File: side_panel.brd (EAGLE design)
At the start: 81.7 x 112 mm, 47 parts

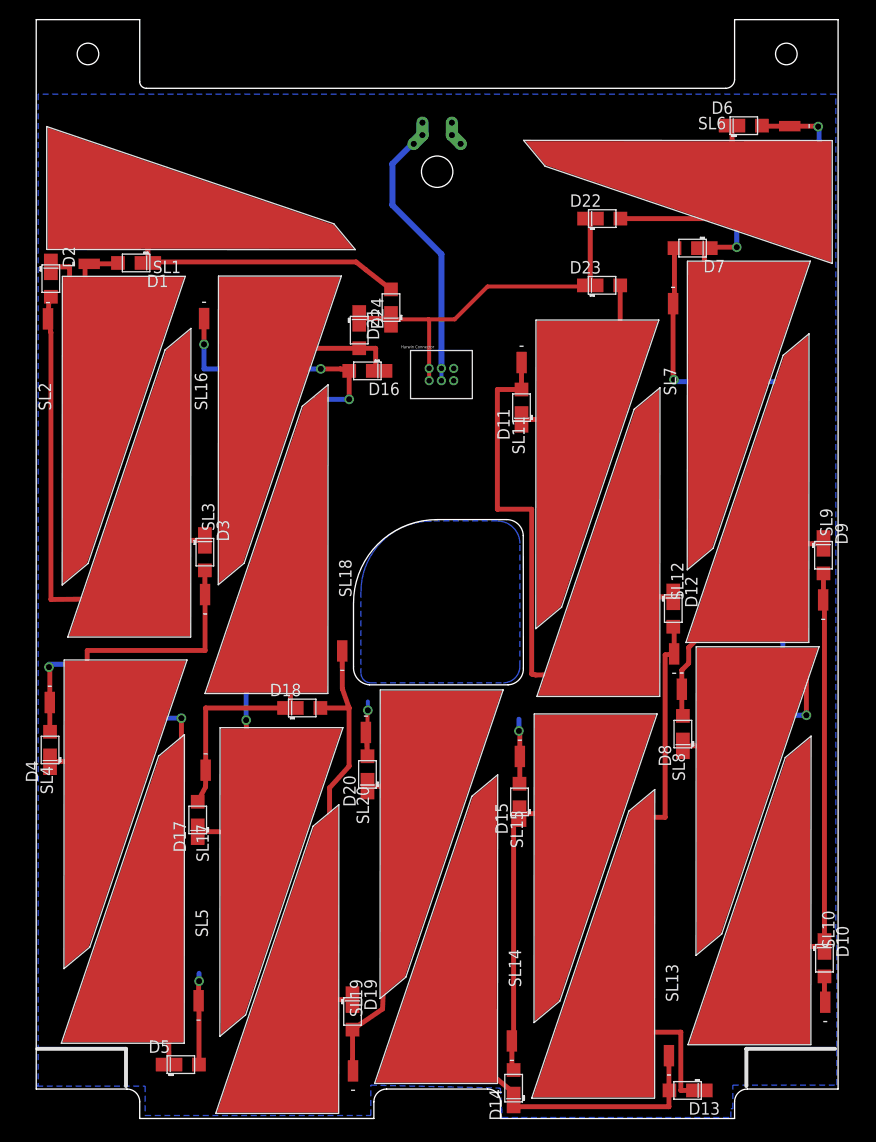
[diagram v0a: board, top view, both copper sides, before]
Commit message: Fixed manufacturing issue on TASC cell footprint
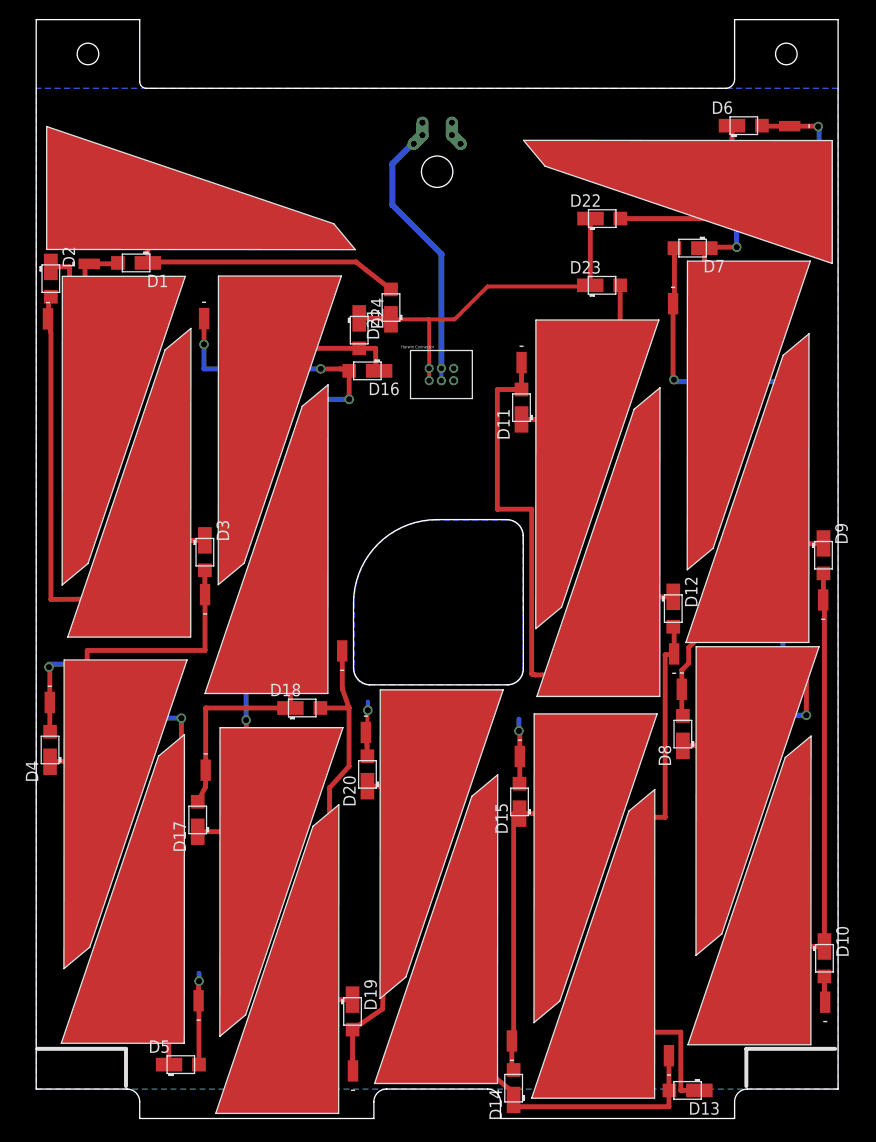
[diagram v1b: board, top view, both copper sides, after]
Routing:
- added copper zone on layer 16, net N$10
- added copper zone on layer 16, net N$12
- removed copper zone on layer 16, net GND
- removed copper zone on layer 16, net N$13
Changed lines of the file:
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@@
 <layers>
 <layer number="1" name="Top" color="4" fill="1" visible="yes" active="yes"/>
+<layer number="2" name="Route2" color="1" fill="3" visible="no" active="no"/>
+<layer number="3" name="Route3" color="4" fill="3" visible="no" active="no"/>
+<layer number="14" name="Route14" color="1" fill="6" visible="no" active="no"/>
+<layer number="15" name="Route15" color="4" fill="6" visible="no" active="no"/>
 <layer number="16" name="Bottom" color="1" fill="1" visible="yes" active="yes"/>
 <layer number="17" name="Pads" color="2" fill="1" visible="yes" active="yes"/>
@@
 <contactref element="SL20" pad="1"/>
 <contactref element="D20" pad="POS"/>
-<polygon width="0" layer="16" thermals="no">
-<vertex x="0.1" y="3.3"/>
-<vertex x="11.1" y="3.3"/>
-<vertex x="11.1" y="0.3"/>
-<vertex x="34.1" y="0.3"/>
-<vertex x="34.1" y="3.4"/>
-<vertex x="47.3" y="3.1"/>
-<vertex x="47.5" y="0.1"/>
-<vertex x="70.8" y="0.1"/>
-<vertex x="70.8" y="1"/>
-<vertex x="71" y="1"/>
-<vertex x="71" y="3.4"/>
-<vertex x="81.6" y="3.4"/>
-<vertex x="81.6" y="19.2"/>
-<vertex x="81.5" y="19.2"/>
-<vertex x="81.5" y="104.4"/>
-<vertex x="0.2" y="104.4"/>
-<vertex x="0.2" y="3.4"/>
-</polygon>
 <wire x1="33.76" y1="36.92" x2="33.66" y2="38.6491" width="0.5" layer="1"/>
 <wire x1="33.66" y1="38.6491" x2="33.6007" y2="39.3491" width="0.5" layer="1"/>
@@
 <contactref element="U$2" pad="H3"/>
 <contactref element="U$2" pad="H1"/>
+<wire x1="42.365" y1="100.23" x2="43.254" y2="99.341" width="0" layer="19" extent="1-1"/>
+<wire x1="42.365" y1="101.5" x2="42.365" y2="100.23" width="0" layer="19" extent="1-1"/>
+<wire x1="42.55" y1="76.45" x2="43.254" y2="99.341" width="0" layer="19" extent="1-1"/>
+<wire x1="42.55" y1="75.2" x2="42.55" y2="76.45" width="0" layer="19" extent="1-1"/>
+<wire x1="33.8" y1="42.5" x2="42.55" y2="75.2" width="0" layer="19" extent="16-16"/>
+<wire x1="49.2" y1="40.7" x2="33.8" y2="41.6" width="0" layer="19" extent="16-16"/>
+<wire x1="16.6" y1="14.8" x2="33.76" y2="36.92" width="0" layer="19" extent="1-16"/>
 </signal>
 <signal name="N$36">
@@
 <wire x1="80.34" y1="11.8509" x2="80.34" y2="14.48" width="0.5" layer="1"/>
 </signal>
-<signal name="N$13">
-<polygon width="0" layer="16" pour="cutout">
-<vertex x="33.1" y="45.9"/>
-<vertex x="33.1" y="45.4" curve="90"/>
-<vertex x="34.1" y="44.4"/>
-<vertex x="47.6" y="44.4" curve="90"/>
-<vertex x="49.3" y="46.1"/>
-<vertex x="49.3" y="58.6" curve="90"/>
-<vertex x="47" y="60.9"/>
-<vertex x="40.3" y="60.9" curve="90"/>
-<vertex x="33.1" y="53.7"/>
-</polygon>
-</signal>
 <signal name="V_BURN">
 <contactref element="U$1" pad="P5"/>
@@
 <wire x1="41.3" y1="88.1" x2="41.3" y2="76.45" width="0.6096" layer="16"/>
 </signal>
+<signal name="N$10">
+<polygon width="0.254" layer="16">
+<vertex x="0" y="3"/>
+<vertex x="81.73" y="3"/>
+<vertex x="81.73" y="105"/>
+<vertex x="0" y="105"/>
+</polygon>
+</signal>
+<signal name="N$12">
+<polygon width="0.254" layer="16" pour="cutout">
+<vertex x="34" y="44.2"/>
+<vertex x="48" y="44.2" curve="90"/>
+<vertex x="49.6" y="45.8"/>
+<vertex x="49.6" y="59.2"/>
+<vertex x="49.6" y="59.4" curve="90"/>
+<vertex x="48" y="61"/>
+<vertex x="40.9" y="61"/>
+<vertex x="40.8" y="61" curve="90"/>
+<vertex x="32.4" y="52.6"/>
+<vertex x="32.4" y="46"/>
+<vertex x="32.4" y="45.7" curve="90"/>
+<vertex x="33.9" y="44.2"/>
+</polygon>
+</signal>
 </signals>

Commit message: Fixed solar panel issue
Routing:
- added copper zone on layer 16, net GND
- removed copper zone on layer 16, net N$10
- removed copper zone on layer 16, net N$12
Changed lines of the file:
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@@
 <?xml version="1.0" encoding="utf-8"?>
 <!DOCTYPE eagle SYSTEM "eagle.dtd">
-<eagle version="6.5.0">
+<eagle version="6.6.0">
 <drawing>
 <settings>
@@
 <contactref element="U$2" pad="H3"/>
 <contactref element="U$2" pad="H1"/>
+<polygon width="0.254" layer="16">
+<vertex x="0" y="3"/>
+<vertex x="81.73" y="3"/>
+<vertex x="81.73" y="105"/>
+<vertex x="0" y="105"/>
+</polygon>
+<polygon width="0.254" layer="16" pour="cutout">
+<vertex x="34" y="44.2"/>
+<vertex x="48" y="44.2" curve="90"/>
+<vertex x="49.6" y="45.8"/>
+<vertex x="49.6" y="59.2"/>
+<vertex x="49.6" y="59.4" curve="90"/>
+<vertex x="48" y="61"/>
+<vertex x="40.9" y="61"/>
+<vertex x="40.8" y="61" curve="90"/>
+<vertex x="32.4" y="52.6"/>
+<vertex x="32.4" y="46"/>
+<vertex x="32.4" y="45.7" curve="90"/>
+<vertex x="33.9" y="44.2"/>
+</polygon>
 <wire x1="42.365" y1="100.23" x2="43.254" y2="99.341" width="0" layer="19" extent="1-1"/>
 <wire x1="42.365" y1="101.5" x2="42.365" y2="100.23" width="0" layer="19" extent="1-1"/>
-<wire x1="42.55" y1="76.45" x2="43.254" y2="99.341" width="0" layer="19" extent="1-1"/>
-<wire x1="42.55" y1="75.2" x2="42.55" y2="76.45" width="0" layer="19" extent="1-1"/>
-<wire x1="33.8" y1="42.5" x2="42.55" y2="75.2" width="0" layer="19" extent="16-16"/>
-<wire x1="49.2" y1="40.7" x2="33.8" y2="41.6" width="0" layer="19" extent="16-16"/>
-<wire x1="16.6" y1="14.8" x2="33.76" y2="36.92" width="0" layer="19" extent="1-16"/>
 </signal>
 <signal name="N$36">
@@
 <wire x1="41.3" y1="88.1" x2="41.3" y2="76.45" width="0.6096" layer="16"/>
 </signal>
-<signal name="N$10">
-<polygon width="0.254" layer="16">
-<vertex x="0" y="3"/>
-<vertex x="81.73" y="3"/>
-<vertex x="81.73" y="105"/>
-<vertex x="0" y="105"/>
-</polygon>
-</signal>
-<signal name="N$12">
-<polygon width="0.254" layer="16" pour="cutout">
-<vertex x="34" y="44.2"/>
-<vertex x="48" y="44.2" curve="90"/>
-<vertex x="49.6" y="45.8"/>
-<vertex x="49.6" y="59.2"/>
-<vertex x="49.6" y="59.4" curve="90"/>
-<vertex x="48" y="61"/>
-<vertex x="40.9" y="61"/>
-<vertex x="40.8" y="61" curve="90"/>
-<vertex x="32.4" y="52.6"/>
-<vertex x="32.4" y="46"/>
-<vertex x="32.4" y="45.7" curve="90"/>
-<vertex x="33.9" y="44.2"/>
-</polygon>
-</signal>
 </signals>

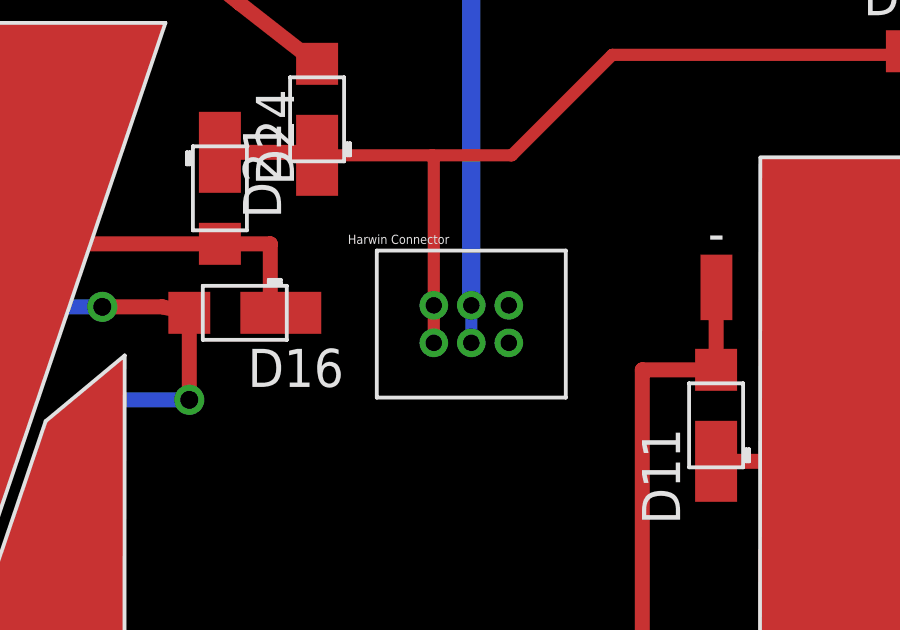
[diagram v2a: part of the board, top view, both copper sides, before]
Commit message: Updated Gecko Connector
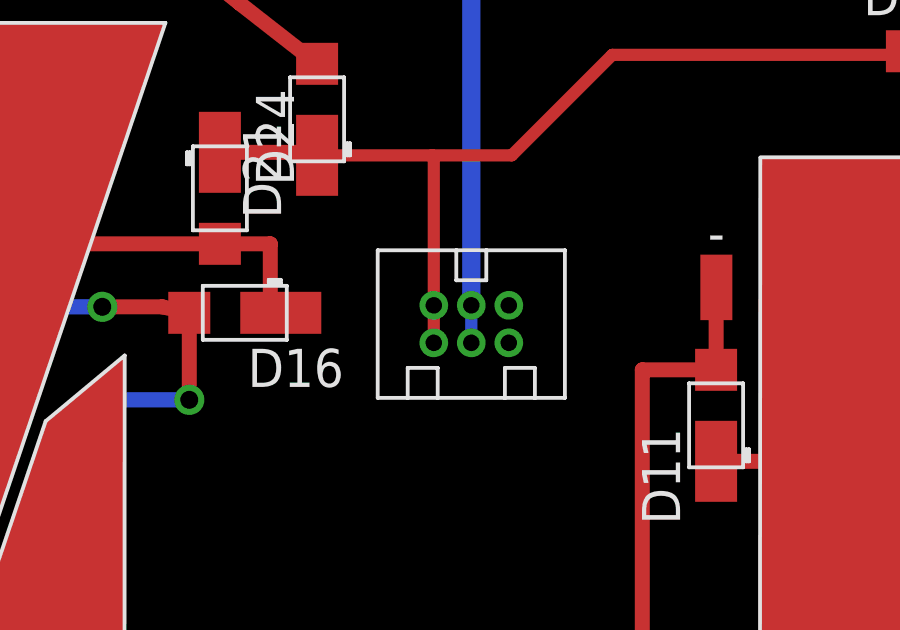
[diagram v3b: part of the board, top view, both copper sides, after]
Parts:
- moved U$1 0.10 mm to (38.2, 73.4)
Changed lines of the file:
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@@
 <element name="D20" library="phonesat" package="SB_DIODE" value="SB_DIODE" x="33.76" y="35.07" rot="R90"/>
 <element name="D24" library="phonesat" package="SB_DIODE" value="SB_DIODE" x="32.92" y="80.35" rot="R270"/>
-<element name="U$1" library="G125-FV20605L0P" package="G125-FV20605L0P" value="G125-FV20605L0P" x="38.1" y="73.3"/>
+<element name="U$1" library="G125-FV20605L0P" package="G125-FV20605L0P" value="G125-FV20605L0P" x="38.18" y="73.365"/>
 <element name="U$4" library="Burner" package="BURNER" value="BURNER" x="39.365" y="101.5" rot="MR270"/>
 <element name="U$2" library="Burner" package="BURNER" value="BURNER" x="42.365" y="101.5" rot="R270"/>

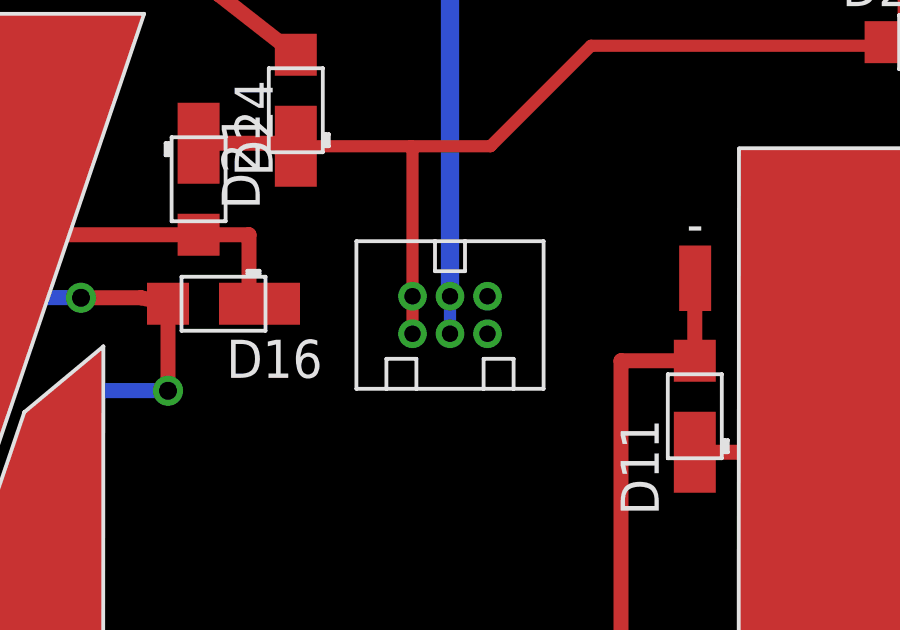
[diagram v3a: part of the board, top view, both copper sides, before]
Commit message: Finished main board layout
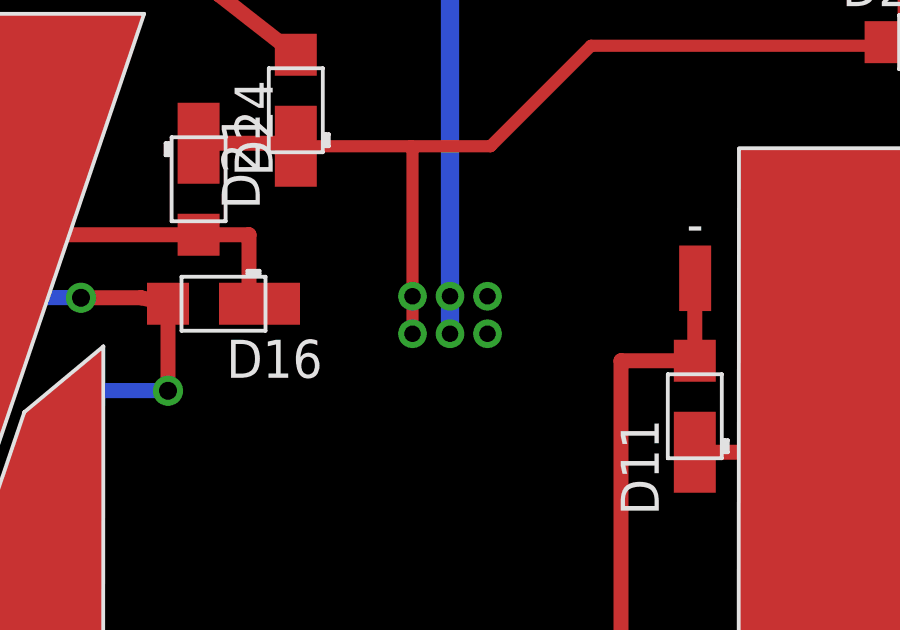
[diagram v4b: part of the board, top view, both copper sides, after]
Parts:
- moved U$1 5.83 mm to (41.3, 78.3), flipped to the bottom, turned to 180 degrees
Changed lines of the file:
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@@
 <element name="D20" library="phonesat" package="SB_DIODE" value="SB_DIODE" x="33.76" y="35.07" rot="R90"/>
 <element name="D24" library="phonesat" package="SB_DIODE" value="SB_DIODE" x="32.92" y="80.35" rot="R270"/>
-<element name="U$1" library="G125-FV20605L0P" package="G125-FV20605L0P" value="G125-FV20605L0P" x="38.18" y="73.365"/>
+<element name="U$1" library="G125-FV20605L0P" package="G125-FV20605L0P" value="G125-FV20605L0P" x="41.3" y="78.285" rot="MR180"/>
 <element name="U$4" library="Burner" package="BURNER" value="BURNER" x="39.365" y="101.5" rot="MR270"/>
 <element name="U$2" library="Burner" package="BURNER" value="BURNER" x="42.365" y="101.5" rot="R270"/>
@@
 <wire x1="56.35" y1="84.8" x2="56.47" y2="84.92" width="0.4064" layer="1"/>
 <wire x1="40.05" y1="81.4" x2="40" y2="81.45" width="0.4064" layer="1"/>
+<contactref element="U$1" pad="P4"/>
 <wire x1="40.05" y1="76.45" x2="40.05" y2="81.4" width="0.4064" layer="1"/>
-<contactref element="U$1" pad="P4"/>
 <wire x1="40.05" y1="76.45" x2="40.05" y2="75.2" width="0.4064" layer="1"/>
 </signal>
@@
 <contactref element="U$1" pad="P5"/>
 <contactref element="U$1" pad="P2"/>
-<wire x1="41.3" y1="75.2" x2="41.3" y2="76.45" width="0.4064" layer="16"/>
 <contactref element="U$4" pad="H2"/>
 <contactref element="U$4" pad="H3"/>
@@
 <wire x1="36.3" y1="93.1" x2="41.3" y2="88.1" width="0.6096" layer="16"/>
 <wire x1="41.3" y1="88.1" x2="41.3" y2="76.45" width="0.6096" layer="16"/>
+<wire x1="41.3" y1="76.45" x2="41.3" y2="75.2" width="0.6096" layer="16"/>
 </signal>
 </signals>

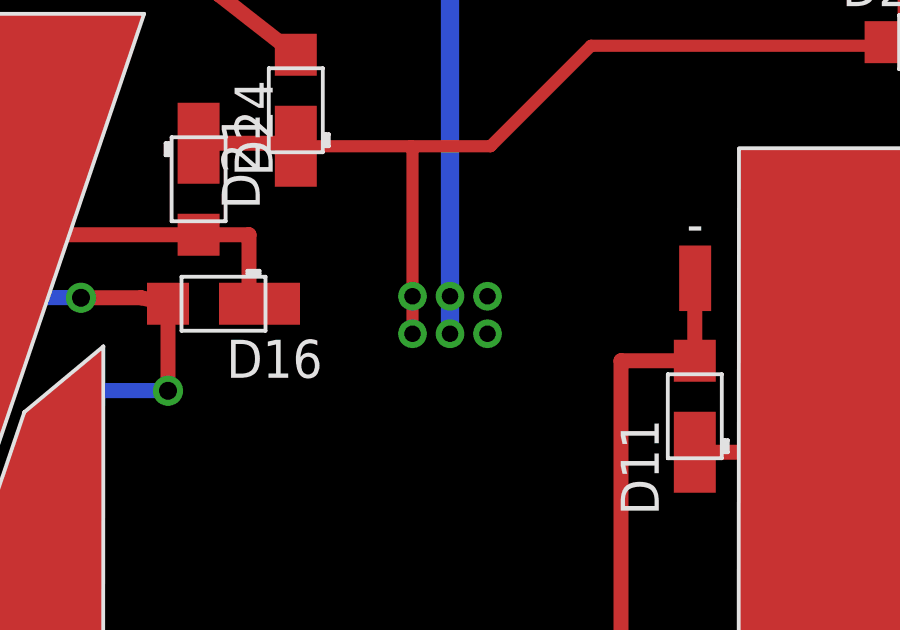
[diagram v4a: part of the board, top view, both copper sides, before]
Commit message: Widened copper around Gecko connector holes
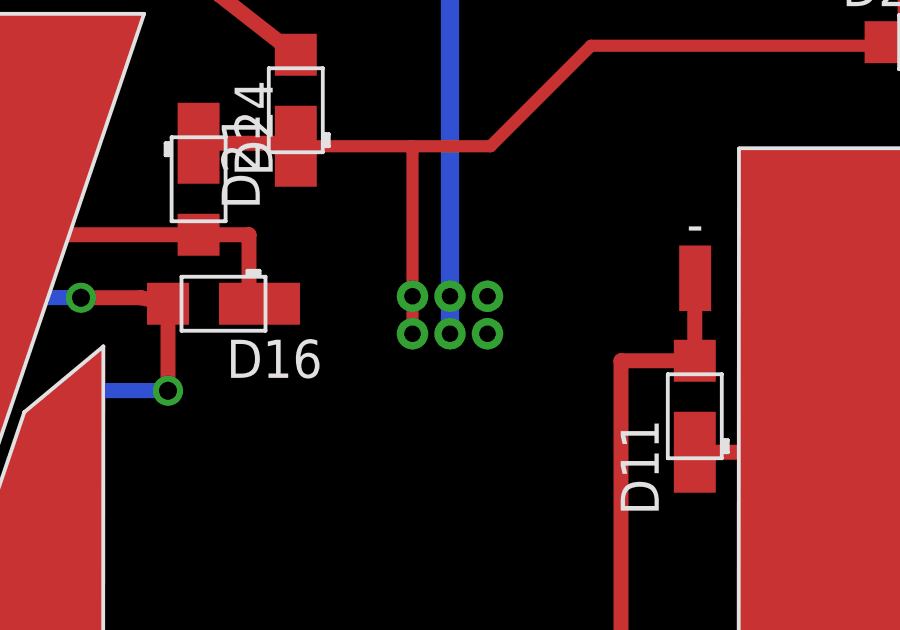
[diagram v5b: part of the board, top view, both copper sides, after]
